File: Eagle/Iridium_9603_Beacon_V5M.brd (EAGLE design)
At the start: 78 x 121 mm, 111 parts, among them CON4 uFL, J1 SS4-10-3.50-X-D, Q1 DMG3415U-7, Q2 DMG3415U-7, Q3 DMG3415U-7, Q4 DMG3415U-7, Q5 2N2222, U1 MCP111T-240E/TT, U2 SPX3819-3.3, U3 LTC3225EDDB#TRMPBF, U4 MPL3115A2LGA8, U5 ATSAMD21G18_QFN, U53 7101K2AV2QE, U6 MAX-M8, U7 LT1634-1,25BMCMS8, X1 32.768

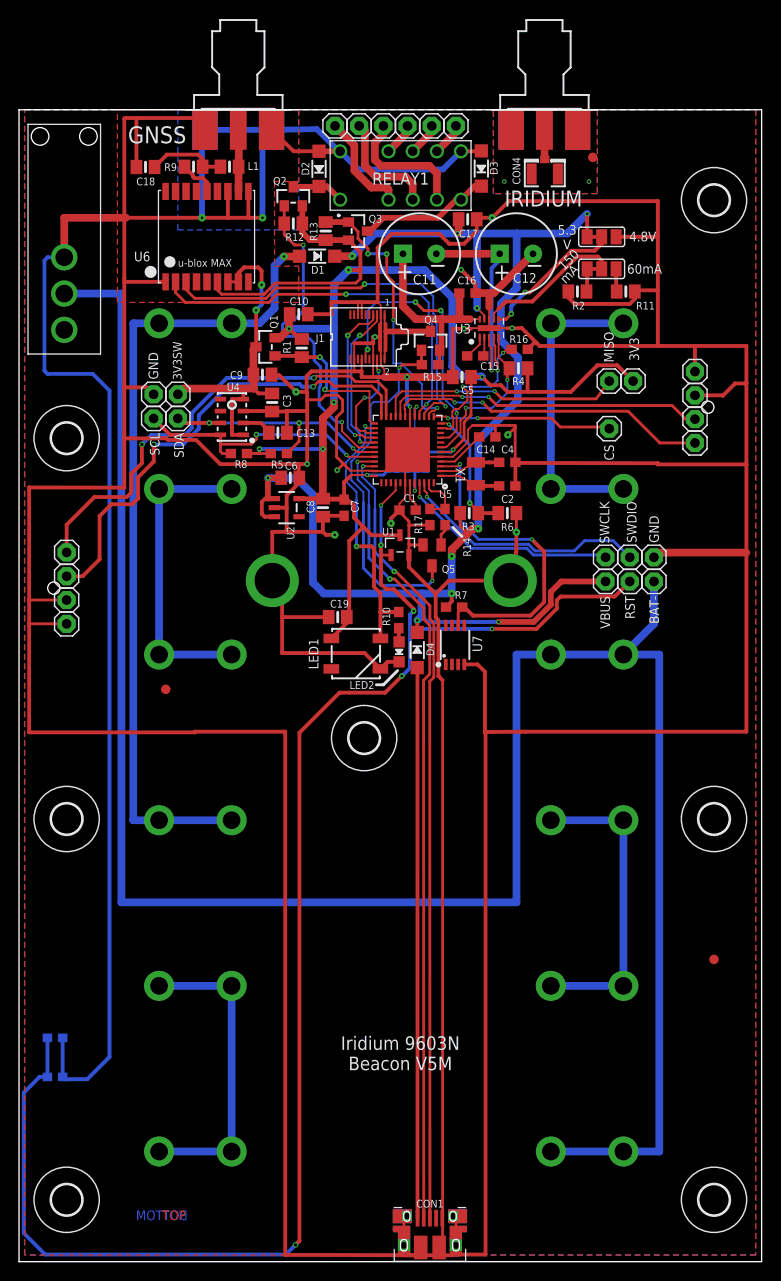
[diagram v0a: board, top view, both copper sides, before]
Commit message: Board layout updated to pass OSH Park rules (mostly)
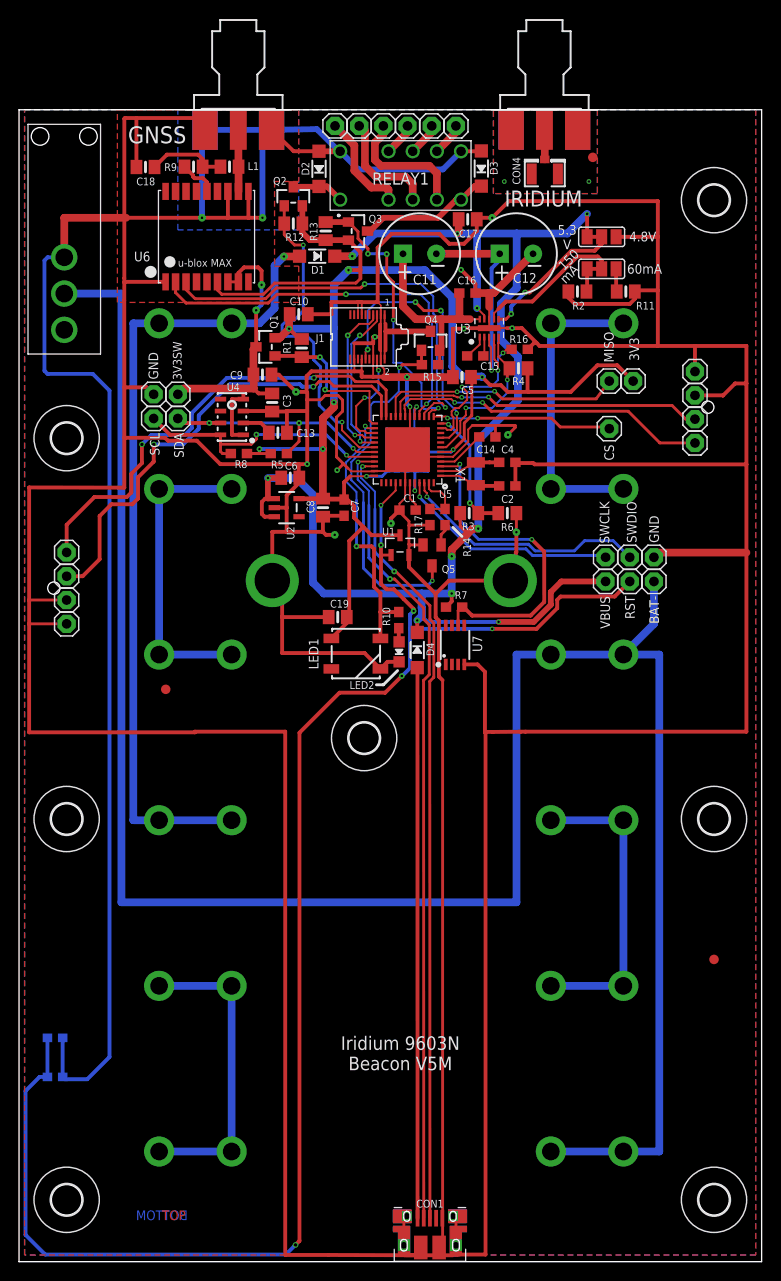
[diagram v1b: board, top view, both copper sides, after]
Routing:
- net GND: track 1012.8 -> 1009.0 mm
